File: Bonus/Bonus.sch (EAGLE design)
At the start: 63 parts, among them U1 CD4094BPW, U2 CD4094BPW, U3 CD4094BPW, U4 MPU-9250

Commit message: Fixed bug in bonus PCB
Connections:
- net SPI-MISO: now also MSP430.14; no longer MSP430.15
- net SPI-MOSI: now also MSP430.15; no longer MSP430.14
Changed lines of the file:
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@@
 <?xml version="1.0" encoding="utf-8"?>
 <!DOCTYPE eagle SYSTEM "eagle.dtd">
-<eagle version="8.4.3">
+<eagle version="9.1.2">
 <drawing>
 <settings>
@@
 <setting verticaltext="up"/>
 </settings>
-<grid distance="0.05" unitdist="inch" unit="inch" style="lines" multiple="2" display="yes" altdistance="0.01" altunitdist="inch" altunit="inch"/>
+<grid distance="0.1" unitdist="inch" unit="inch" style="lines" multiple="1" display="no" altdistance="0.01" altunitdist="inch" altunit="inch"/>
 <layers>
 <layer number="1" name="Top" color="4" fill="1" visible="no" active="no"/>
@@
 <net name="SPI-MISO" class="0">
 <segment>
-<pinref part="MSP430" gate="G$1" pin="15"/>
-<wire x1="25.4" y1="-2.54" x2="48.26" y2="-2.54" width="0.1524" layer="91"/>
-<label x="38.1" y="-2.54" size="1.778" layer="95"/>
-</segment>
-<segment>
 <pinref part="U4" gate="G$1" pin="AD0/SDO"/>
 <wire x1="-100.33" y1="10.16" x2="-109.22" y2="10.16" width="0.1524" layer="91"/>
 <label x="-110.49" y="10.16" size="1.778" layer="95"/>
 </segment>
+<segment>
+<pinref part="MSP430" gate="G$1" pin="14"/>
+<wire x1="25.4" y1="-5.08" x2="50.8" y2="-5.08" width="0.1524" layer="91"/>
+<label x="45.72" y="-5.08" size="1.778" layer="95"/>
+</segment>
 </net>
 <net name="SPI-MOSI" class="0">
-<segment>
-<pinref part="MSP430" gate="G$1" pin="14"/>
-<wire x1="25.4" y1="-5.08" x2="48.26" y2="-5.08" width="0.1524" layer="91"/>
-<label x="38.1" y="-5.08" size="1.778" layer="95"/>
-</segment>
 <segment>
 <pinref part="U4" gate="G$1" pin="SDA/SDI"/>
@@
 <label x="-67.31" y="30.48" size="1.778" layer="95"/>
 </segment>
-</net>
+<segment>
+<pinref part="MSP430" gate="G$1" pin="15"/>
+<wire x1="25.4" y1="-2.54" x2="50.8" y2="-2.54" width="0.1524" layer="91"/>
+<label x="45.72" y="-2.54" size="1.778" layer="95"/>
+</segment>
+</net>

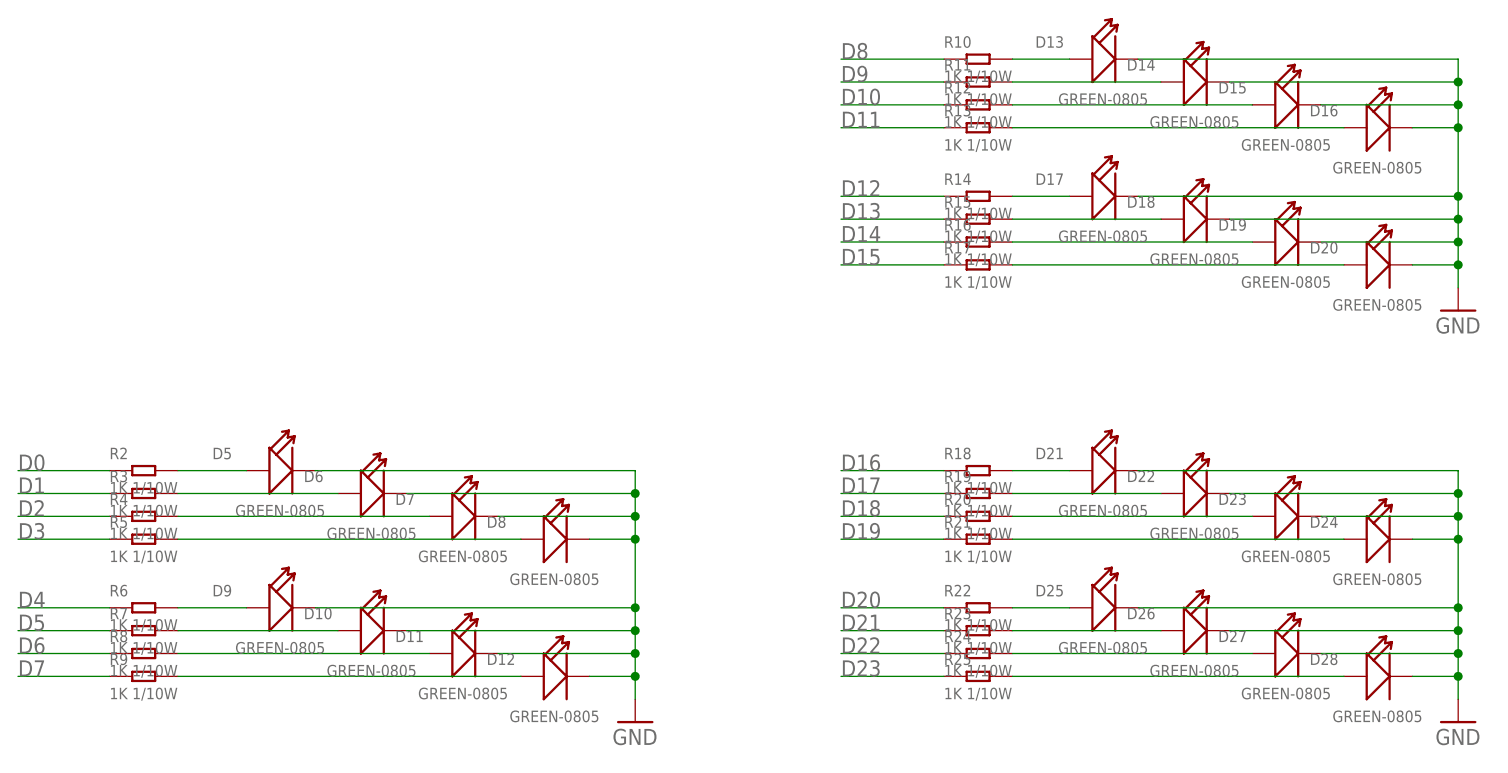
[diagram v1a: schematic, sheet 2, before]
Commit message: Updated LED resistors from 1K to 300 ohms
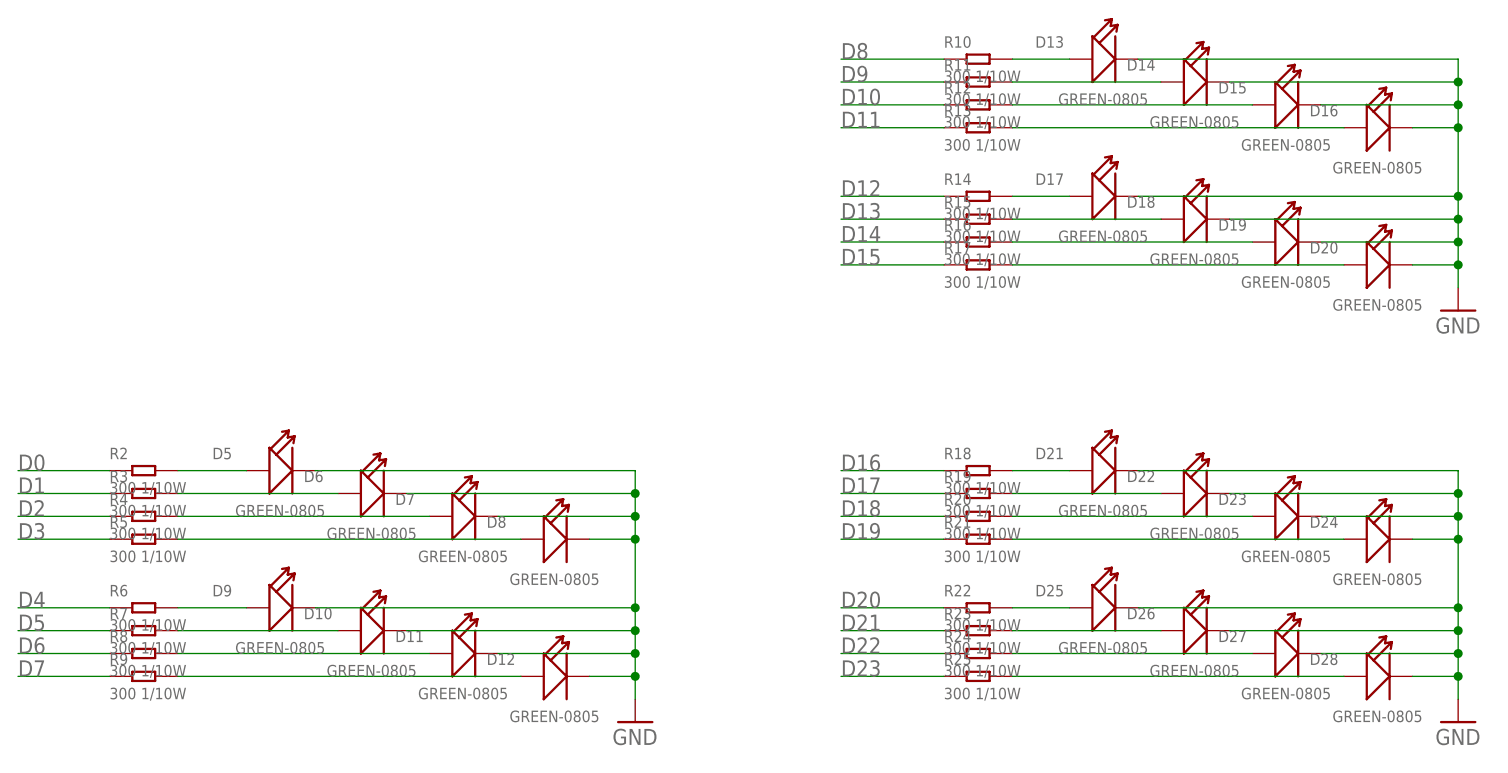
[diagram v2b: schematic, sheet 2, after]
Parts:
- R10, R11, R12, R13, R14, R15, R16, R17, R18, R19, R2, R20, R21, R22, R23, R24, R25, R3, R4, R5, R6, R7, R8, R9: value 1K 1/10W -> 300 1/10W

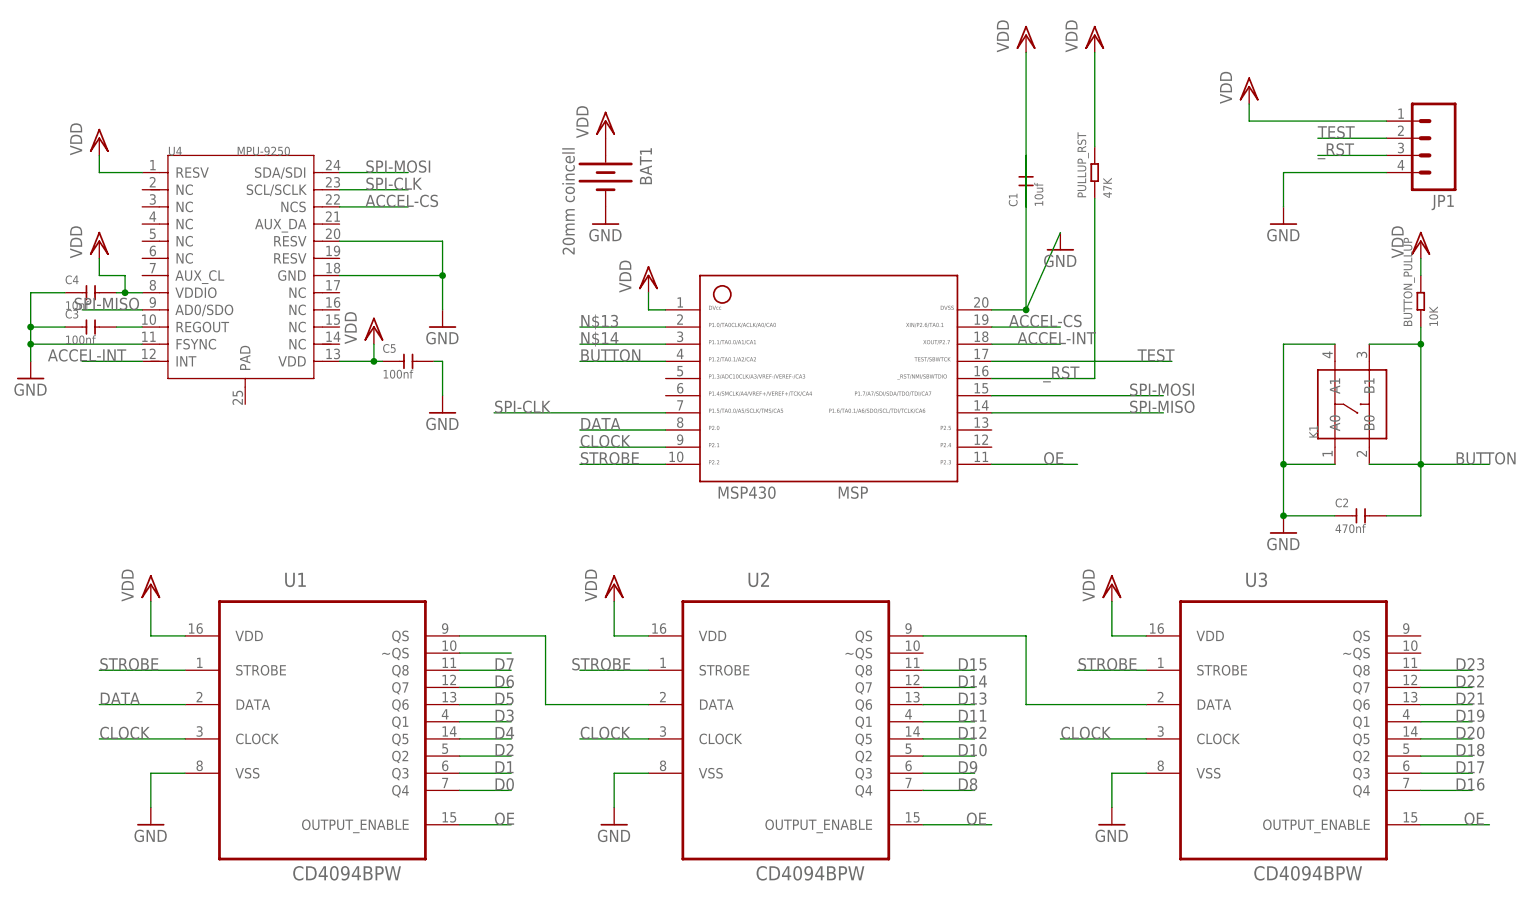
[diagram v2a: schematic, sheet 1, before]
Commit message: Moved Lab3 to Lab4 and added new RGB LED. Also updated Bonus PCB for manufacturing
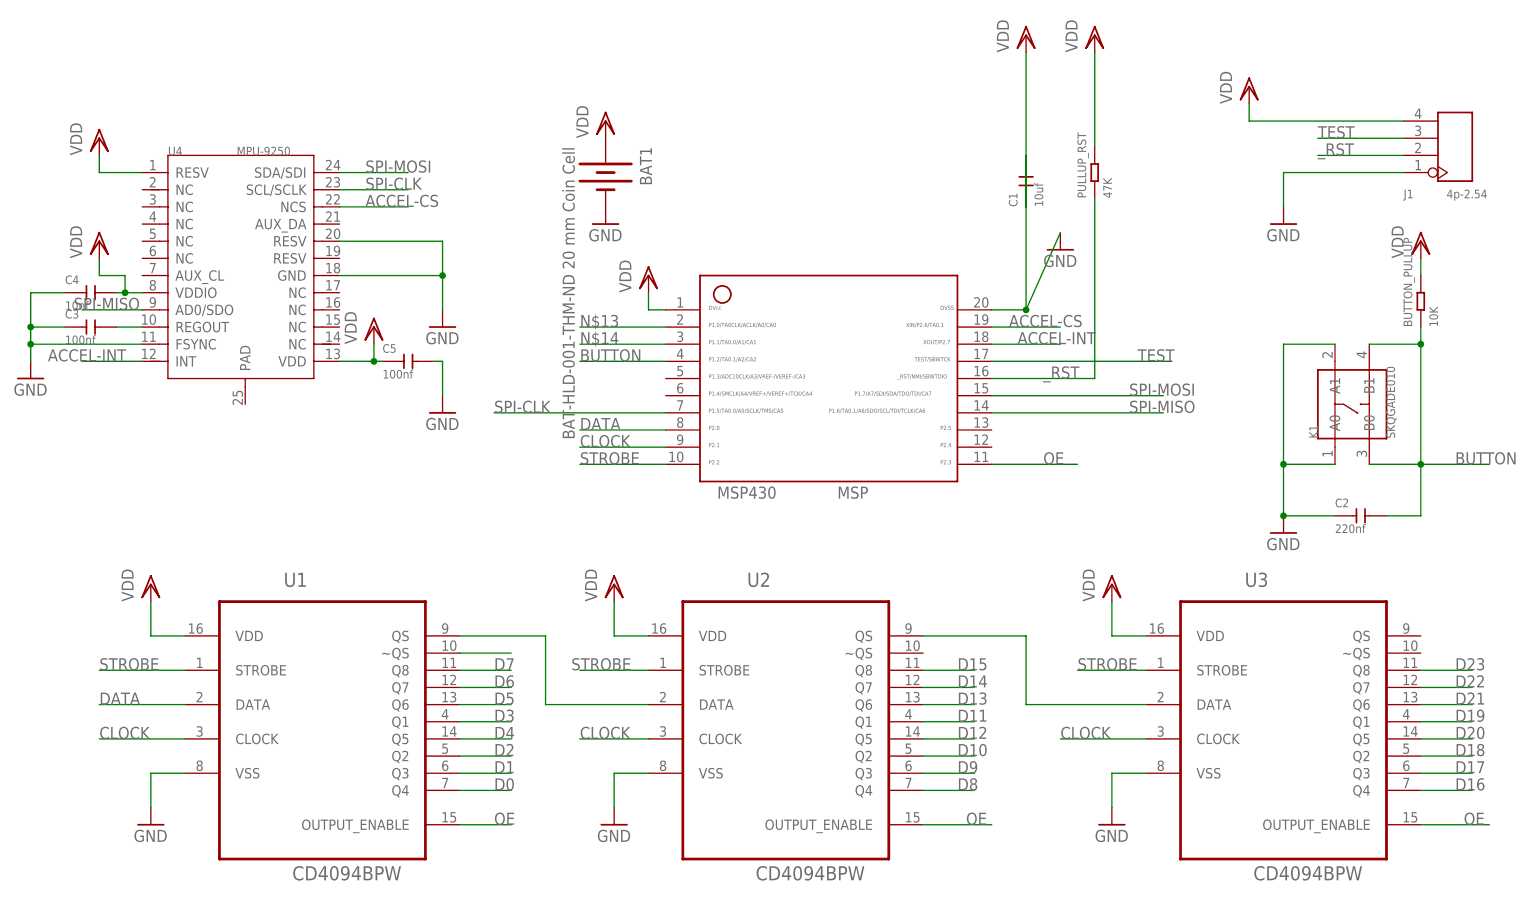
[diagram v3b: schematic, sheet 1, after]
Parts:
- removed JP1: (no value), Pendant:M04LOCK
- added J1: 4p-2.54, OPL_Connector:DIP-BLACK-FEMALE-HEADER-VERT(4P-2.54)
- BAT1: value 20mm coincell -> BAT-HLD-001-THM-ND 20 mm Coin Cell
- C2: value 470nf -> 220nf; device Seeed-OPL-Capacitor:CERAMIC-470NF-25V-10%-X7R(0603) -> OPL_Capacitor:CERAMIC-220NF-25V-10%-X7R(0603)
- K1: value (none) -> SKQGADE010; device Seeed-OPL-Switch:SMD-SWITCH-TACTILE-SPST-NO(4P-D6.0MM) -> OPL_Switch:SMD-BUTTON(4P-5.2X5.2X1.5MM-SKQGADE010)-SKQGADE010
- R10, R11, R12, R13, R14, R15, R16, R17, R18, R19, R2, R20, R21, R22, R23, R24, R25, R3, R4, R5, R6, R7, R8, R9: value 300 1/10W -> 390R; device Seeed-OPL-Resistor:SMD-RES-1K-5%-1/10W(0603) -> OPL_Resistor:SMD-RES-390R-5%-1/10W(0603)
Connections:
- net GND: now also J1.P$1; no longer JP1.4
- net TEST: now also J1.P$3; no longer JP1.2
- net VDD: now also J1.P$4; no longer JP1.1
- net _RST: now also J1.P$2; no longer JP1.3
